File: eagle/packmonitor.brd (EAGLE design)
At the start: 100 x 80 mm, 7 parts, among them IC2 24C64, J1 UPDI_COMPACT

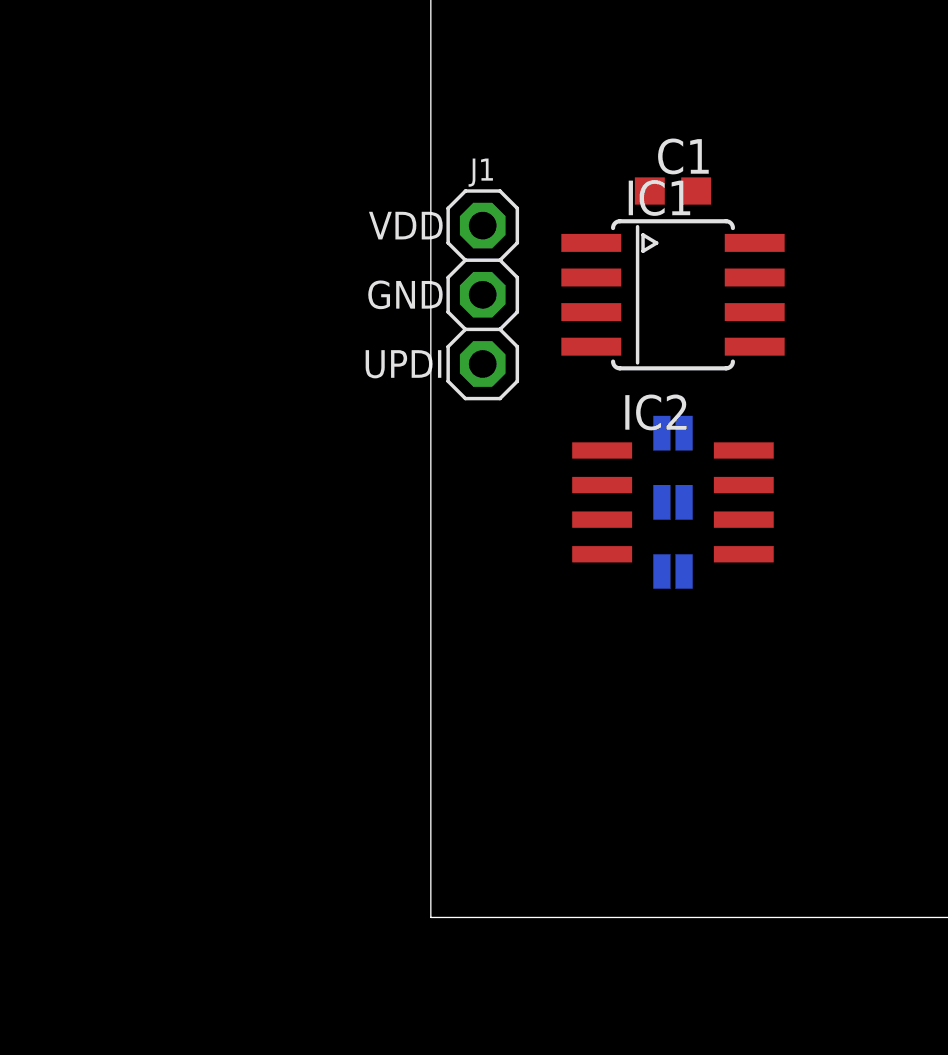
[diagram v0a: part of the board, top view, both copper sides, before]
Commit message: added 4808 mcu
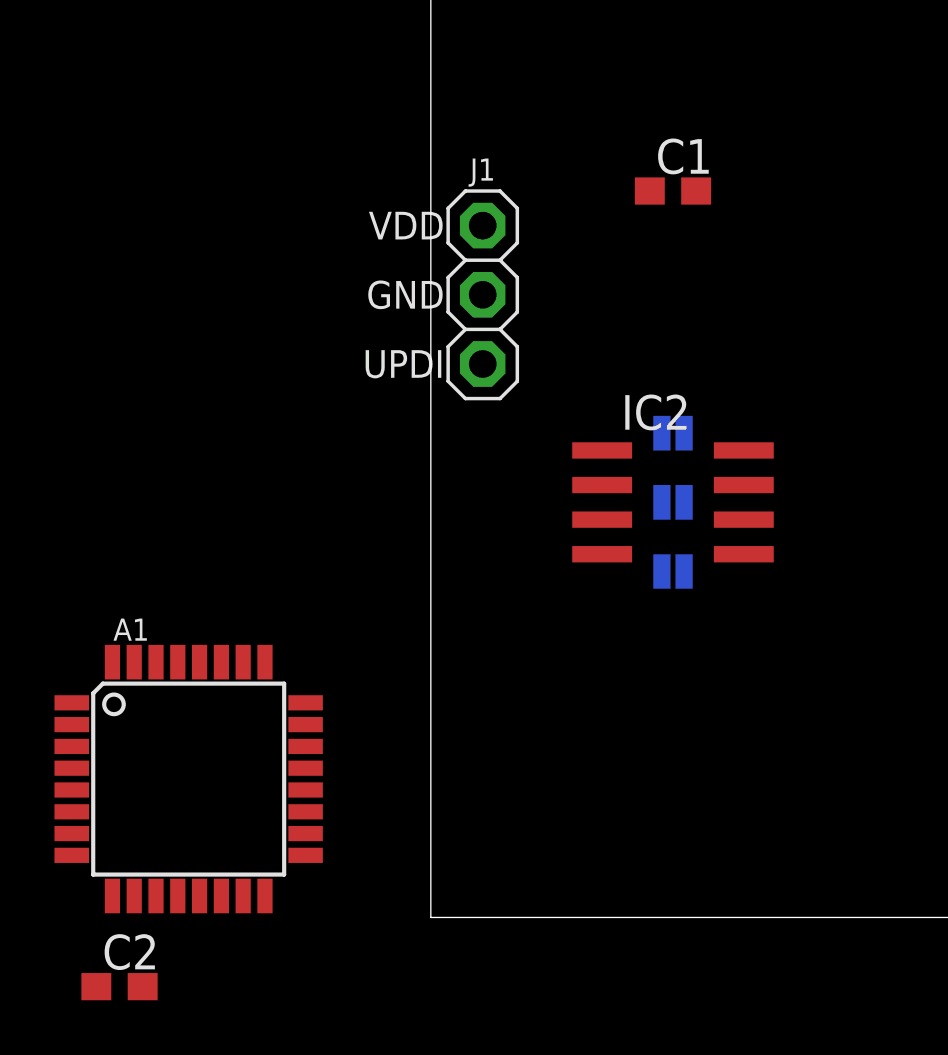
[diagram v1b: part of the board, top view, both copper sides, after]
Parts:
- removed IC1: (no value), bt_avr:SOIC8N
- added A1: ATMEGA4808-TQFN32A, microchip-special:TQFP32-08
- added C2: 100u, rcl:C0603
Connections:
- new net N$2: A1.18, C2.1
- net GND: now also A1.19, A1.29, C2.2; no longer IC1.8
- net N$1: no longer IC1.6
- net SCL: no longer IC1.5
- net SDA: no longer IC1.4
- net VCC: now also A1.28; no longer IC1.1
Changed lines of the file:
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@@
 <elements>
 <element name="C1" library="rcl" package="C0603" value="100u" x="8.89" y="26.67"/>
-<element name="IC1" library="bt_avr" package="SOIC8N" value="" x="8.89" y="22.86" rot="R270"/>
 <element name="J1" library="bt_avr" package="UPDI_1X3" value="UPDI_COMPACT" x="1.905" y="22.86"/>
 <element name="IC2" library="microchip" package="SO-08" value="24C64" x="8.89" y="15.24" rot="R270">
@@
 <element name="JP2" library="SparkFun-Jumpers" package="SMT-JUMPER_2_NO_SILK" value="A1" x="8.89" y="15.24" rot="MR0"/>
 <element name="JP3" library="SparkFun-Jumpers" package="SMT-JUMPER_2_NO_SILK" value="A2" x="8.89" y="12.7" rot="MR0"/>
+<element name="A1" library="microchip-special" package="TQFP32-08" value="ATMEGA4808-TQFN32A" x="-8.89" y="5.08"/>
+<element name="C2" library="rcl" package="C0603" value="100u" x="-11.43" y="-2.54"/>
 </elements>
 <signals>
 <signal name="N$1">
 <contactref element="J1" pad="3"/>
-<contactref element="IC1" pad="6"/>
-<wire x1="1.905" y1="20.32" x2="11.89" y2="22.225" width="0" layer="19" extent="1-1"/>
 </signal>
 <signal name="VCC">
 <contactref element="J1" pad="1"/>
-<contactref element="IC1" pad="1"/>
-<contactref element="C1" pad="1"/>
 <contactref element="IC2" pad="8"/>
 <contactref element="JP1" pad="1"/>
 <contactref element="JP2" pad="1"/>
 <contactref element="JP3" pad="1"/>
-<wire x1="5.89" y1="24.765" x2="8.04" y2="26.67" width="0" layer="19" extent="1-1"/>
-<wire x1="1.905" y1="25.4" x2="5.89" y2="24.765" width="0" layer="19" extent="1-1"/>
-<wire x1="9.2964" y1="17.78" x2="5.89" y2="24.765" width="0" layer="19" extent="1-16"/>
+<contactref element="A1" pad="28"/>
+<contactref element="C1" pad="1"/>
+<wire x1="1.905" y1="25.4" x2="8.04" y2="26.67" width="0" layer="19" extent="1-1"/>
+<wire x1="9.2964" y1="17.78" x2="8.04" y2="26.67" width="0" layer="19" extent="1-16"/>
 <wire x1="11.49" y1="17.145" x2="9.2964" y2="17.78" width="0" layer="19" extent="1-16"/>
 <wire x1="9.2964" y1="15.24" x2="9.2964" y2="17.78" width="0" layer="19" extent="16-16"/>
 <wire x1="9.2964" y1="12.7" x2="9.2964" y2="15.24" width="0" layer="19" extent="16-16"/>
+<wire x1="-8.49" y1="9.3726" x2="9.2964" y2="12.7" width="0" layer="19" extent="1-16"/>
 </signal>
 <signal name="GND">
-<contactref element="IC1" pad="8"/>
-<contactref element="C1" pad="2"/>
 <contactref element="J1" pad="2"/>
 <contactref element="IC2" pad="4"/>
 <contactref element="IC2" pad="7"/>
-<wire x1="9.74" y1="26.67" x2="11.89" y2="24.765" width="0" layer="19" extent="1-1"/>
+<contactref element="A1" pad="19"/>
+<contactref element="A1" pad="29"/>
+<contactref element="C1" pad="2"/>
+<contactref element="C2" pad="2"/>
 <wire x1="1.905" y1="22.86" x2="9.74" y2="26.67" width="0" layer="19" extent="1-1"/>
-<wire x1="11.49" y1="15.875" x2="11.89" y2="24.765" width="0" layer="19" extent="1-1"/>
-<wire x1="6.29" y1="13.335" x2="11.49" y2="15.875" width="0" layer="19" extent="1-1"/>
+<wire x1="6.29" y1="13.335" x2="1.905" y2="22.86" width="0" layer="19" extent="1-1"/>
+<wire x1="11.49" y1="15.875" x2="6.29" y2="13.335" width="0" layer="19" extent="1-1"/>
+<wire x1="-4.5974" y1="3.88" x2="6.29" y2="13.335" width="0" layer="19" extent="1-1"/>
+<wire x1="-9.29" y1="9.3726" x2="-4.5974" y2="3.88" width="0" layer="19" extent="1-1"/>
+<wire x1="-10.58" y1="-2.54" x2="-4.5974" y2="3.88" width="0" layer="19" extent="1-1"/>
 </signal>
 <signal name="A0">
@@
 </signal>
 <signal name="SDA">
-<contactref element="IC1" pad="4"/>
 <contactref element="IC2" pad="5"/>
-<wire x1="11.49" y1="13.335" x2="5.89" y2="20.955" width="0" layer="19" extent="1-1"/>
 </signal>
 <signal name="SCL">
-<contactref element="IC1" pad="5"/>
 <contactref element="IC2" pad="6"/>
-<wire x1="11.49" y1="14.605" x2="11.89" y2="20.955" width="0" layer="19" extent="1-1"/>
+</signal>
+<signal name="N$2">
+<contactref element="A1" pad="18"/>
+<contactref element="C2" pad="1"/>
+<wire x1="-4.5974" y1="3.08" x2="-12.28" y2="-2.54" width="0" layer="19" extent="1-1"/>
 </signal>
 </signals>

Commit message: slowly adding parts and putting together layout
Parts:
- added C3: 100u, rcl:C0603
- J1: value UPDI_COMPACT -> (none); device bt_avr:UPDI_1X3 -> SparkFun-Connectors:1X03_LOCK_LONGPADS
- moved C2 64.2 mm to (50.0, 16.0), turned to 180 degrees
- moved A1 59.0 mm to (50.0, 9.00)
- moved IC2 57.4 mm to (66.0, 9.00)
- moved JP2 57.4 mm to (66.0, 9.20)
- moved JP1 57.4 mm to (66.0, 11.8)
- moved JP3 57.4 mm to (66.0, 7.00)
- moved C1 52.5 mm to (58.0, 8.00), turned to 90 degrees
- moved J1 38.1 mm to (36.6, 7.11)
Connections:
- removed net N$1: J1.3
- net GND: now also C3.2, J1.1; no longer J1.2
- net N$2: now also A1.27, J1.2; no longer A1.18, C2.1
- net SCL: now also A1.1
- net SDA: now also A1.32
- net VCC: now also A1.18, C2.1, C3.1, J1.3; no longer J1.1
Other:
- board size 100 x 80 mm -> 100 x 18 mm
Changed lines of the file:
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@@
 <setting verticaltext="up"/>
 </settings>
-<grid distance="0.05" unitdist="inch" unit="inch" style="lines" multiple="1" display="no" altdistance="0.025" altunitdist="inch" altunit="inch"/>
+<grid distance="1" unitdist="mm" unit="mm" style="lines" multiple="1" display="no" altdistance="0.2" altunitdist="mm" altunit="mm"/>
 <layers>
 <layer number="1" name="Top" color="4" fill="1" visible="yes" active="yes"/>
@@
 <plain>
 <wire x1="0" y1="0" x2="100" y2="0" width="0" layer="20"/>
-<wire x1="100" y1="0" x2="100" y2="80" width="0" layer="20"/>
-<wire x1="100" y1="80" x2="0" y2="80" width="0" layer="20"/>
-<wire x1="0" y1="80" x2="0" y2="0" width="0" layer="20"/>
+<wire x1="100" y1="0" x2="100" y2="18" width="0" layer="20"/>
+<wire x1="100" y1="18" x2="0" y2="18" width="0" layer="20"/>
+<wire x1="0" y1="18" x2="0" y2="0" width="0" layer="20"/>
 </plain>
 <attributes>
@@
 </autorouter>
 <elements>
-<element name="C1" library="rcl" package="C0603" value="100u" x="8.89" y="26.67"/>
-<element name="J1" library="bt_avr" package="UPDI_1X3" value="UPDI_COMPACT" x="1.905" y="22.86"/>
-<element name="IC2" library="microchip" package="SO-08" value="24C64" x="8.89" y="15.24" rot="R270">
-<attribute name="MF" value="" x="8.89" y="15.24" size="1.778" layer="27" rot="R270" display="off"/>
-<attribute name="MPN" value="" x="8.89" y="15.24" size="1.778" layer="27" rot="R270" display="off"/>
-<attribute name="OC_FARNELL" value="unknown" x="8.89" y="15.24" size="1.778" layer="27" rot="R270" display="off"/>
-<attribute name="OC_NEWARK" value="unknown" x="8.89" y="15.24" size="1.778" layer="27" rot="R270" display="off"/>
+<element name="C1" library="rcl" package="C0603" value="100u" x="58" y="8" rot="R90"/>
+<element name="IC2" library="microchip" package="SO-08" value="24C64" x="66" y="9" rot="R270">
+<attribute name="MF" value="" x="66" y="9" size="1.778" layer="27" rot="R270" display="off"/>
+<attribute name="MPN" value="" x="66" y="9" size="1.778" layer="27" rot="R270" display="off"/>
+<attribute name="OC_FARNELL" value="unknown" x="66" y="9" size="1.778" layer="27" rot="R270" display="off"/>
+<attribute name="OC_NEWARK" value="unknown" x="66" y="9" size="1.778" layer="27" rot="R270" display="off"/>
 </element>
-<element name="JP1" library="SparkFun-Jumpers" package="SMT-JUMPER_2_NO_SILK" value="A)" x="8.89" y="17.78" rot="MR0"/>
-<element name="JP2" library="SparkFun-Jumpers" package="SMT-JUMPER_2_NO_SILK" value="A1" x="8.89" y="15.24" rot="MR0"/>
-<element name="JP3" library="SparkFun-Jumpers" package="SMT-JUMPER_2_NO_SILK" value="A2" x="8.89" y="12.7" rot="MR0"/>
-<element name="A1" library="microchip-special" package="TQFP32-08" value="ATMEGA4808-TQFN32A" x="-8.89" y="5.08"/>
-<element name="C2" library="rcl" package="C0603" value="100u" x="-11.43" y="-2.54"/>
+<element name="JP1" library="SparkFun-Jumpers" package="SMT-JUMPER_2_NO_SILK" value="A)" x="66" y="11.8" rot="MR0"/>
+<element name="JP2" library="SparkFun-Jumpers" package="SMT-JUMPER_2_NO_SILK" value="A1" x="66" y="9.2" rot="MR0"/>
+<element name="JP3" library="SparkFun-Jumpers" package="SMT-JUMPER_2_NO_SILK" value="A2" x="66" y="7" rot="MR0"/>
+<element name="A1" library="microchip-special" package="TQFP32-08" value="ATMEGA4808-TQFN32A" x="50" y="9"/>
+<element name="C2" library="rcl" package="C0603" value="100u" x="50" y="16" rot="R180"/>
+<element name="J1" library="SparkFun-Connectors" package="1X03_LOCK_LONGPADS" value="" x="36.57" y="7.11"/>
+<element name="C3" library="rcl" package="C0603" value="100u" x="66" y="15"/>
 </elements>
 <signals>
-<signal name="N$1">
-<contactref element="J1" pad="3"/>
-</signal>
 <signal name="VCC">
-<contactref element="J1" pad="1"/>
 <contactref element="IC2" pad="8"/>
 <contactref element="JP1" pad="1"/>
@@
 <contactref element="A1" pad="28"/>
 <contactref element="C1" pad="1"/>
-<wire x1="1.905" y1="25.4" x2="8.04" y2="26.67" width="0" layer="19" extent="1-1"/>
-<wire x1="9.2964" y1="17.78" x2="8.04" y2="26.67" width="0" layer="19" extent="1-16"/>
-<wire x1="11.49" y1="17.145" x2="9.2964" y2="17.78" width="0" layer="19" extent="1-16"/>
-<wire x1="9.2964" y1="15.24" x2="9.2964" y2="17.78" width="0" layer="19" extent="16-16"/>
-<wire x1="9.2964" y1="12.7" x2="9.2964" y2="15.24" width="0" layer="19" extent="16-16"/>
-<wire x1="-8.49" y1="9.3726" x2="9.2964" y2="12.7" width="0" layer="19" extent="1-16"/>
+<contactref element="C2" pad="1"/>
+<contactref element="A1" pad="18"/>
+<contactref element="J1" pad="3"/>
+<contactref element="C3" pad="1"/>
+<wire x1="66.4064" y1="11.8" x2="68.6" y2="10.905" width="0" layer="19" extent="1-16"/>
+<wire x1="66.4064" y1="9.2" x2="66.4064" y2="11.8" width="0" layer="19" extent="16-16"/>
+<wire x1="66.4064" y1="7" x2="66.4064" y2="9.2" width="0" layer="19" extent="16-16"/>
+<wire x1="65.15" y1="15" x2="66.4064" y2="11.8" width="0" layer="19" extent="1-16"/>
+<wire x1="58" y1="7.15" x2="66.4064" y2="7" width="0" layer="19" extent="1-16"/>
+<wire x1="54.2926" y1="7" x2="58" y2="7.15" width="0" layer="19" extent="1-1"/>
+<wire x1="50.4" y1="13.2926" x2="54.2926" y2="7" width="0" layer="19" extent="1-1"/>
+<wire x1="50.85" y1="16" x2="50.4" y2="13.2926" width="0" layer="19" extent="1-1"/>
+<wire x1="41.65" y1="7.11" x2="50.4" y2="13.2926" width="0" layer="19" extent="1-1"/>
 </signal>
 <signal name="GND">
-<contactref element="J1" pad="2"/>
 <contactref element="IC2" pad="4"/>
 <contactref element="IC2" pad="7"/>
@@
 <contactref element="C1" pad="2"/>
 <contactref element="C2" pad="2"/>
-<wire x1="1.905" y1="22.86" x2="9.74" y2="26.67" width="0" layer="19" extent="1-1"/>
-<wire x1="6.29" y1="13.335" x2="1.905" y2="22.86" width="0" layer="19" extent="1-1"/>
-<wire x1="11.49" y1="15.875" x2="6.29" y2="13.335" width="0" layer="19" extent="1-1"/>
-<wire x1="-4.5974" y1="3.88" x2="6.29" y2="13.335" width="0" layer="19" extent="1-1"/>
-<wire x1="-9.29" y1="9.3726" x2="-4.5974" y2="3.88" width="0" layer="19" extent="1-1"/>
-<wire x1="-10.58" y1="-2.54" x2="-4.5974" y2="3.88" width="0" layer="19" extent="1-1"/>
+<contactref element="J1" pad="1"/>
+<contactref element="C3" pad="2"/>
+<wire x1="68.6" y1="9.635" x2="66.85" y2="15" width="0" layer="19" extent="1-1"/>
+<wire x1="63.4" y1="7.095" x2="68.6" y2="9.635" width="0" layer="19" extent="1-1"/>
+<wire x1="58" y1="8.85" x2="63.4" y2="7.095" width="0" layer="19" extent="1-1"/>
+<wire x1="54.2926" y1="7.8" x2="58" y2="8.85" width="0" layer="19" extent="1-1"/>
+<wire x1="49.6" y1="13.2926" x2="54.2926" y2="7.8" width="0" layer="19" extent="1-1"/>
+<wire x1="49.15" y1="16" x2="49.6" y2="13.2926" width="0" layer="19" extent="1-1"/>
+<wire x1="36.57" y1="7.11" x2="49.6" y2="13.2926" width="0" layer="19" extent="1-1"/>
 </signal>
 <signal name="A0">
 <contactref element="IC2" pad="1"/>
 <contactref element="JP1" pad="2"/>
-<wire x1="6.29" y1="17.145" x2="8.4836" y2="17.78" width="0" layer="19" extent="1-16"/>
+<wire x1="63.4" y1="10.905" x2="65.5936" y2="11.8" width="0" layer="19" extent="1-16"/>
 </signal>
 <signal name="A1">
 <contactref element="IC2" pad="2"/>
 <contactref element="JP2" pad="2"/>
-<wire x1="6.29" y1="15.875" x2="8.4836" y2="15.24" width="0" layer="19" extent="1-16"/>
+<wire x1="63.4" y1="9.635" x2="65.5936" y2="9.2" width="0" layer="19" extent="1-16"/>
 </signal>
 <signal name="A2">
 <contactref element="IC2" pad="3"/>
 <contactref element="JP3" pad="2"/>
-<wire x1="6.29" y1="14.605" x2="8.4836" y2="12.7" width="0" layer="19" extent="1-16"/>
+<wire x1="65.5936" y1="7" x2="63.4" y2="8.365" width="0" layer="19" extent="1-16"/>
 </signal>
 <signal name="SDA">
 <contactref element="IC2" pad="5"/>
+<contactref element="A1" pad="32"/>
+<wire x1="47.2" y1="13.2926" x2="68.6" y2="7.095" width="0" layer="19" extent="1-1"/>
 </signal>
 <signal name="SCL">
 <contactref element="IC2" pad="6"/>
+<contactref element="A1" pad="1"/>
+<wire x1="45.7074" y1="11.8" x2="68.6" y2="8.365" width="0" layer="19" extent="1-1"/>
 </signal>
 <signal name="N$2">
-<contactref element="A1" pad="18"/>
-<contactref element="C2" pad="1"/>
-<wire x1="-4.5974" y1="3.08" x2="-12.28" y2="-2.54" width="0" layer="19" extent="1-1"/>
+<contactref element="J1" pad="2"/>
+<contactref element="A1" pad="27"/>
+<wire x1="39.11" y1="6.856" x2="51.2" y2="13.2926" width="0" layer="19" extent="1-1"/>
 </signal>
 </signals>
